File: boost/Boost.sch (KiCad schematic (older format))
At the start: 17 parts

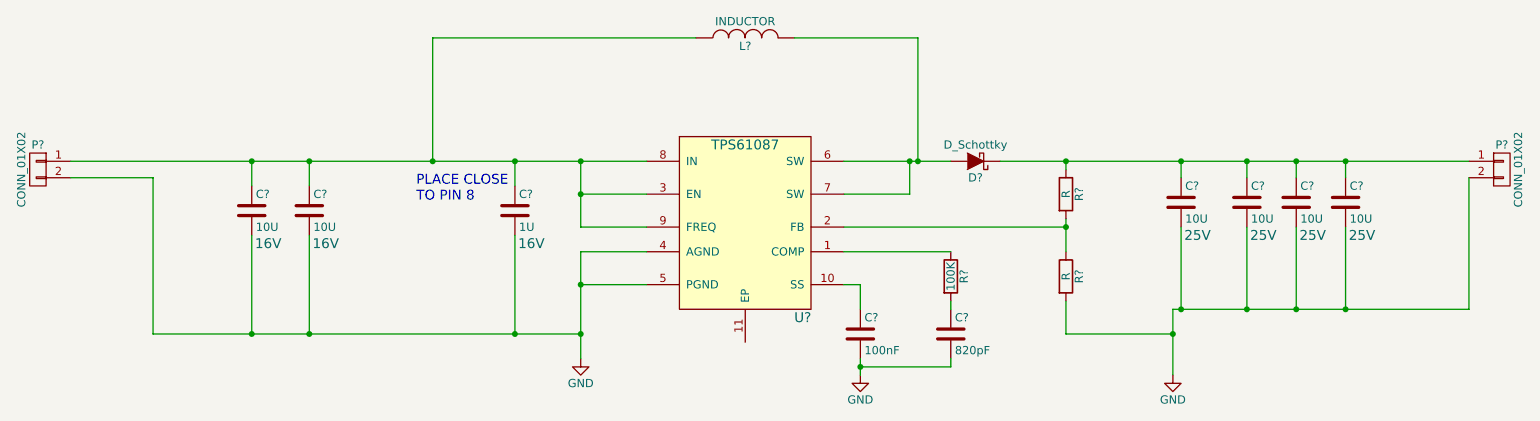
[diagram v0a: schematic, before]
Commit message: Added footprints to layout
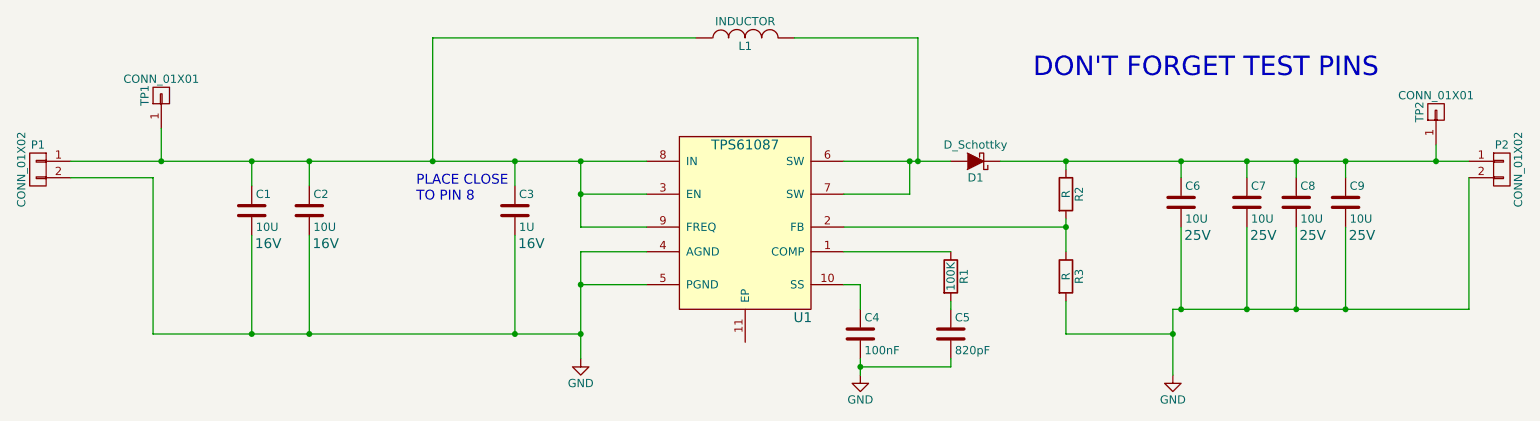
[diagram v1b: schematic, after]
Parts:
- added TP1, TP2: CONN_01X01, Measurement_Points:Measurement_Point_Square-SMD-Pad_Big, symbol CONN_01X01
- C1, C2, C6, C7, C8, C9: renamed from C?; footprint (none) -> Capacitors_SMD:C_1206_HandSoldering
- C3, C4, C5: renamed from C?; footprint (none) -> Capacitors_SMD:C_0805_HandSoldering
- D1: renamed from D?; footprint (none) -> Diodes_SMD:SMA-SMB_Universal_Handsoldering
- P1, P2: renamed from P?; footprint (none) -> Pin_Headers:Pin_Header_Straight_1x02
- R1, R2, R3: renamed from R?; footprint (none) -> Resistors_SMD:R_0805_HandSoldering
- gave numbers to parts that had none: 2
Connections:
- net at C1.1, C2.1, C3.1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: now also TP1.1 (P1)
- net at C6.1, C7.1, C8.1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: now also TP2.1 (P1)
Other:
- note added: "DON'T FORGET TEST PINS"
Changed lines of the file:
@@
 LIBS:valves
 LIBS:Boost-PowerSwap
+LIBS:Boost-cache
 EELAYER 25 0
 EELAYER END
@@
 $EndDescr
 $Comp
-L TPS61087 U?
+L TPS61087 U1
 U 1 1 56319256
 P 5600 3750
-F 0 "U?" H 5950 3200 60  0000 C CNN
+F 0 "U1" H 5950 3200 60  0000 C CNN
 F 1 "TPS61087" H 5600 4250 60  0000 C CNN
-F 2 "" H 5600 3600 60  0000 C CNN
+F 2 "" H 5600 3600 60  0001 C CNN
 F 3 "" H 5600 3600 60  0000 C CNN
 	1    5600 3750
@@
 $EndComp
 $Comp
-L INDUCTOR L?
+L INDUCTOR L1
 U 1 1 563192CC
 P 5600 2600
-F 0 "L?" V 5550 2600 50  0000 C CNN
+F 0 "L1" V 5550 2600 50  0000 C CNN
 F 1 "INDUCTOR" V 5700 2600 50  0000 C CNN
-F 2 "" H 5600 2600 60  0000 C CNN
+F 2 "" H 5600 2600 60  0001 C CNN
 F 3 "" H 5600 2600 60  0000 C CNN
 	1    5600 2600
@@
 $EndComp
 $Comp
-L GND #PWR?
+L GND #PWR01
 U 1 1 56319311
 P 4600 4550
-F 0 "#PWR?" H 4600 4300 50  0001 C CNN
+F 0 "#PWR01" H 4600 4300 50  0001 C CNN
 F 1 "GND" H 4600 4400 50  0000 C CNN
 F 2 "" H 4600 4550 60  0000 C CNN
@@
 $EndComp
 $Comp
-L C C?
+L C C1
 U 1 1 56319465
 P 2600 3650
-F 0 "C?" H 2625 3750 50  0000 L CNN
+F 0 "C1" H 2625 3750 50  0000 L CNN
 F 1 "10U" H 2625 3550 50  0000 L CNN
-F 2 "" H 2638 3500 30  0000 C CNN
+F 2 "Capacitors_SMD:C_1206_HandSoldering" H 2638 3500 30  0001 C CNN
 F 3 "" H 2600 3650 60  0000 C CNN
 F 4 "16V" H 2700 3450 60  0000 C CNN "Voltage"
@@
 $EndComp
 $Comp
-L C C?
+L C C2
 U 1 1 56319636
 P 2950 3650
-F 0 "C?" H 2975 3750 50  0000 L CNN
+F 0 "C2" H 2975 3750 50  0000 L CNN
 F 1 "10U" H 2975 3550 50  0000 L CNN
-F 2 "" H 2988 3500 30  0000 C CNN
+F 2 "Capacitors_SMD:C_1206_HandSoldering" H 2988 3500 30  0001 C CNN
 F 3 "" H 2950 3650 60  0000 C CNN
 F 4 "16V" H 3050 3450 60  0000 C CNN "Voltage"
@@
 $EndComp
 $Comp
-L C C?
+L C C3
 U 1 1 5631988E
 P 4200 3650
-F 0 "C?" H 4225 3750 50  0000 L CNN
+F 0 "C3" H 4225 3750 50  0000 L CNN
 F 1 "1U" H 4225 3550 50  0000 L CNN
-F 2 "" H 4238 3500 30  0000 C CNN
+F 2 "Capacitors_SMD:C_0805_HandSoldering" H 4238 3500 30  0001 C CNN
 F 3 "" H 4200 3650 60  0000 C CNN
 F 4 "16V" H 4300 3450 60  0000 C CNN "Voltage"
@@
 PLACE CLOSE\nTO PIN 8\n
 $Comp
-L CONN_01X02 P?
+L CONN_01X02 P1
 U 1 1 56319D59
 P 1300 3400
-F 0 "P?" H 1300 3550 50  0000 C CNN
+F 0 "P1" H 1300 3550 50  0000 C CNN
 F 1 "CONN_01X02" V 1400 3400 50  0000 C CNN
-F 2 "" H 1300 3400 60  0000 C CNN
+F 2 "Pin_Headers:Pin_Header_Straight_1x02" H 1300 3400 60  0001 C CNN
 F 3 "" H 1300 3400 60  0000 C CNN
 	1    1300 3400
@@
 $EndComp
 $Comp
-L C C?
+L C C6
 U 1 1 5631A40E
 P 8250 3600
-F 0 "C?" H 8275 3700 50  0000 L CNN
+F 0 "C6" H 8275 3700 50  0000 L CNN
 F 1 "10U" H 8275 3500 50  0000 L CNN
-F 2 "" H 8288 3450 30  0000 C CNN
+F 2 "Capacitors_SMD:C_1206_HandSoldering" H 8288 3450 30  0001 C CNN
 F 3 "" H 8250 3600 60  0000 C CNN
 F 4 "25V" H 8350 3400 60  0000 C CNN "Voltage"
@@
 $EndComp
 $Comp
-L C C?
+L C C7
 U 1 1 5631A62E
 P 8650 3600
-F 0 "C?" H 8675 3700 50  0000 L CNN
+F 0 "C7" H 8675 3700 50  0000 L CNN
 F 1 "10U" H 8675 3500 50  0000 L CNN
-F 2 "" H 8688 3450 30  0000 C CNN
+F 2 "Capacitors_SMD:C_1206_HandSoldering" H 8688 3450 30  0001 C CNN
 F 3 "" H 8650 3600 60  0000 C CNN
 F 4 "25V" H 8750 3400 60  0000 C CNN "Voltage"
@@
 $EndComp
 $Comp
-L C C?
+L C C8
 U 1 1 5631A664
 P 8950 3600
-F 0 "C?" H 8975 3700 50  0000 L CNN
+F 0 "C8" H 8975 3700 50  0000 L CNN
 F 1 "10U" H 8975 3500 50  0000 L CNN
-F 2 "" H 8988 3450 30  0000 C CNN
+F 2 "Capacitors_SMD:C_1206_HandSoldering" H 8988 3450 30  0001 C CNN
 F 3 "" H 8950 3600 60  0000 C CNN
 F 4 "25V" H 9050 3400 60  0000 C CNN "Voltage"
@@
 $EndComp
 $Comp
-L C C?
+L C C9
 U 1 1 5631A699
 P 9250 3600
-F 0 "C?" H 9275 3700 50  0000 L CNN
+F 0 "C9" H 9275 3700 50  0000 L CNN
 F 1 "10U" H 9275 3500 50  0000 L CNN
-F 2 "" H 9288 3450 30  0000 C CNN
+F 2 "Capacitors_SMD:C_1206_HandSoldering" H 9288 3450 30  0001 C CNN
 F 3 "" H 9250 3600 60  0000 C CNN
 F 4 "25V" H 9350 3400 60  0000 C CNN "Voltage"
@@
 $EndComp
 $Comp
-L GND #PWR?
+L GND #PWR02
 U 1 1 5631AB38
 P 8200 4650
-F 0 "#PWR?" H 8200 4400 50  0001 C CNN
+F 0 "#PWR02" H 8200 4400 50  0001 C CNN
 F 1 "GND" H 8200 4500 50  0000 C CNN
 F 2 "" H 8200 4650 60  0000 C CNN
@@
 $EndComp
 $Comp
-L R R?
+L R R2
 U 1 1 5631ACD8
 P 7550 3550
-F 0 "R?" V 7630 3550 50  0000 C CNN
+F 0 "R2" V 7630 3550 50  0000 C CNN
 F 1 "R" V 7550 3550 50  0000 C CNN
-F 2 "" V 7480 3550 30  0000 C CNN
+F 2 "Resistors_SMD:R_0805_HandSoldering" V 7480 3550 30  0001 C CNN
 F 3 "" H 7550 3550 30  0000 C CNN
 	1    7550 3550
@@
 $EndComp
 $Comp
-L R R?
+L R R3
 U 1 1 5631AD24
 P 7550 4050
-F 0 "R?" V 7630 4050 50  0000 C CNN
+F 0 "R3" V 7630 4050 50  0000 C CNN
 F 1 "R" V 7550 4050 50  0000 C CNN
-F 2 "" V 7480 4050 30  0000 C CNN
+F 2 "Resistors_SMD:R_0805_HandSoldering" V 7480 4050 30  0001 C CNN
 F 3 "" H 7550 4050 30  0000 C CNN
 	1    7550 4050
@@
 Connection ~ 7550 3750
 $Comp
-L C C?
+L C C4
 U 1 1 5631B263
 P 6300 4400
-F 0 "C?" H 6325 4500 50  0000 L CNN
+F 0 "C4" H 6325 4500 50  0000 L CNN
 F 1 "100nF" H 6325 4300 50  0000 L CNN
-F 2 "" H 6338 4250 30  0000 C CNN
+F 2 "Capacitors_SMD:C_0805_HandSoldering" H 6338 4250 30  0001 C CNN
 F 3 "" H 6300 4400 60  0000 C CNN
 	1    6300 4400
@@
 	6300 4100 6200 4100
 $Comp
-L GND #PWR?
+L GND #PWR03
 U 1 1 5631B351
 P 6300 4650
-F 0 "#PWR?" H 6300 4400 50  0001 C CNN
+F 0 "#PWR03" H 6300 4400 50  0001 C CNN
 F 1 "GND" H 6300 4500 50  0000 C CNN
 F 2 "" H 6300 4650 60  0000 C CNN
@@
 	6300 4550 6300 4650
 $Comp
-L C C?
+L C C5
 U 1 1 5631B401
 P 6850 4400
-F 0 "C?" H 6875 4500 50  0000 L CNN
+F 0 "C5" H 6875 4500 50  0000 L CNN
 F 1 "820pF" H 6875 4300 50  0000 L CNN
-F 2 "" H 6888 4250 30  0000 C CNN
+F 2 "Capacitors_SMD:C_0805_HandSoldering" H 6888 4250 30  0001 C CNN
 F 3 "" H 6850 4400 60  0000 C CNN
 	1    6850 4400
@@
 $EndComp
 $Comp
-L R R?
+L R R1
 U 1 1 5631B45F
 P 6850 4050
-F 0 "R?" V 6930 4050 50  0000 C CNN
+F 0 "R1" V 6930 4050 50  0000 C CNN
 F 1 "100K" V 6850 4050 50  0000 C CNN
-F 2 "" V 6780 4050 30  0000 C CNN
+F 2 "Resistors_SMD:R_0805_HandSoldering" V 6780 4050 30  0001 C CNN
 F 3 "" H 6850 4050 30  0000 C CNN
 	1    6850 4050
@@
 Connection ~ 6300 4600
 $Comp
-L D_Schottky D?
+L D_Schottky D1
 U 1 1 5631C97C
 P 7000 3350
-F 0 "D?" H 7000 3450 50  0000 C CNN
+F 0 "D1" H 7000 3450 50  0000 C CNN
 F 1 "D_Schottky" H 7000 3250 50  0000 C CNN
-F 2 "" H 7000 3350 60  0000 C CNN
+F 2 "Diodes_SMD:SMA-SMB_Universal_Handsoldering" H 7000 3350 60  0001 C CNN
 F 3 "" H 7000 3350 60  0000 C CNN
 	1    7000 3350
@@
 $EndComp
 $Comp
-L CONN_01X02 P?
+L CONN_01X02 P2
 U 1 1 5631CEDA
 P 10200 3400
-F 0 "P?" H 10200 3550 50  0000 C CNN
+F 0 "P2" H 10200 3550 50  0000 C CNN
 F 1 "CONN_01X02" V 10300 3400 50  0000 C CNN
-F 2 "" H 10200 3400 60  0000 C CNN
+F 2 "Pin_Headers:Pin_Header_Straight_1x02" H 10200 3400 60  0001 C CNN
 F 3 "" H 10200 3400 60  0000 C CNN
 	1    10200 3400
@@
 	10000 4250 10000 3450
 Connection ~ 9250 4250
+Text Notes 7350 2850 0    118  ~ 0
+DON'T FORGET TEST PINS
+$Comp
+L CONN_01X01 TP1
+U 1 1 5636B9F0
+P 2050 2950
+F 0 "TP1" H 2050 3050 50  0000 C CNN
+F 1 "CONN_01X01" V 2150 2950 50  0000 C CNN
+F 2 "Measurement_Points:Measurement_Point_Square-SMD-Pad_Big" H 2050 2950 60  0001 C CNN
+F 3 "" H 2050 2950 60  0000 C CNN
+	1    2050 2950
+	0    -1   -1   0
+$EndComp
+$Comp
+L CONN_01X01 TP2
+U 1 1 5636BC69
+P 9800 3050
+F 0 "TP2" H 9800 3150 50  0000 C CNN
+F 1 "CONN_01X01" V 9900 3050 50  0000 C CNN
+F 2 "Measurement_Points:Measurement_Point_Square-SMD-Pad_Big" H 9800 3050 60  0001 C CNN
+F 3 "" H 9800 3050 60  0000 C CNN
+	1    9800 3050
+	0    -1   -1   0
+$EndComp
+Wire Wire Line
+	9800 3250 9800 3350
+Connection ~ 9800 3350
+Wire Wire Line
+	2050 3150 2050 3350
+Connection ~ 2050 3350
 $EndSCHEMATC

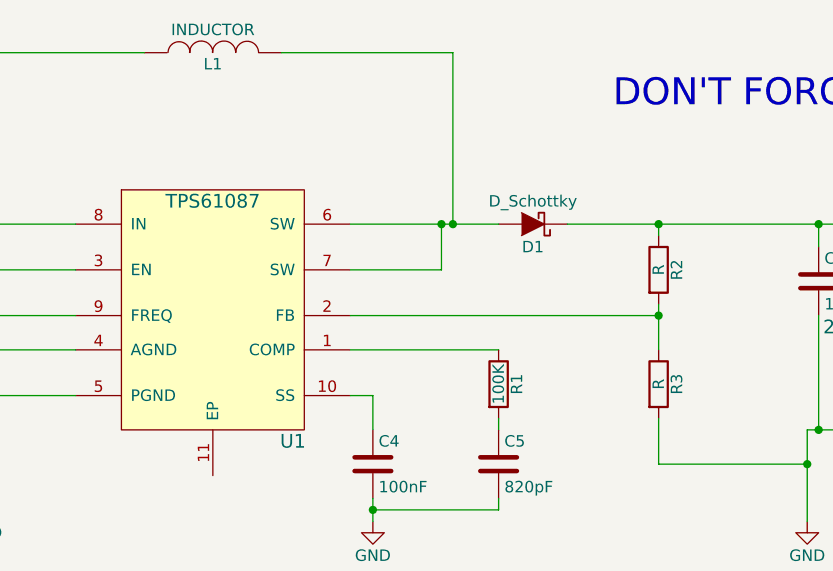
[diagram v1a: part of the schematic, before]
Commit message: Updated component values
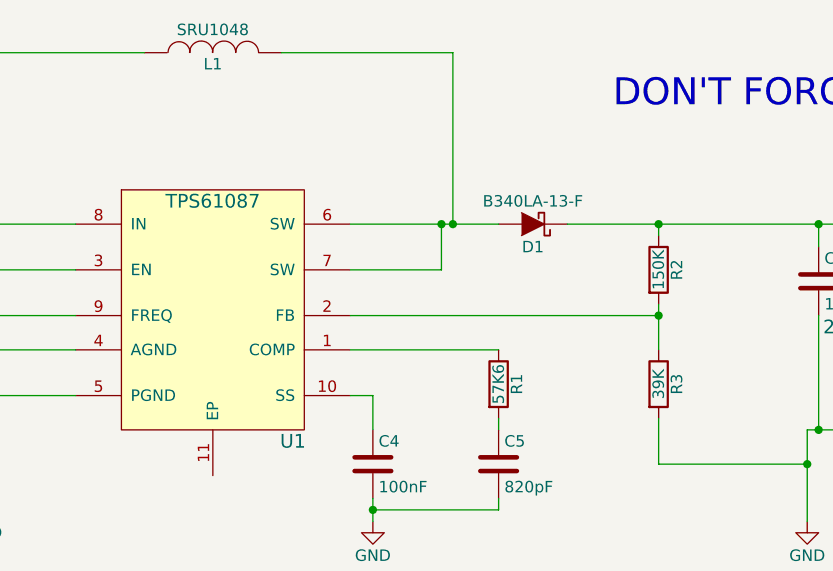
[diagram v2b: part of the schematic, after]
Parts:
- D1: value D_Schottky -> B340LA-13-F; MPN (none) -> B340LA-13-F
- L1: value INDUCTOR -> SRU1048; footprint (none) -> Boost:SRU1048; MPN (none) -> SRU1048-4R7Y
- R1: value 100K -> 57K6
- R2: value R -> 150K
- R3: value R -> 39K
- U1: footprint (none) -> Boost:TPS61087; MPN (none) -> TPS61087QDRCRQ1
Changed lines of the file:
@@
 F 0 "U1" H 5950 3200 60  0000 C CNN
 F 1 "TPS61087" H 5600 4250 60  0000 C CNN
-F 2 "" H 5600 3600 60  0001 C CNN
+F 2 "Boost:TPS61087" H 5600 3600 60  0001 C CNN
 F 3 "" H 5600 3600 60  0000 C CNN
+F 4 "TPS61087QDRCRQ1" H 5600 3750 60  0001 C CNN "MPN"
 	1    5600 3750
 	1    0    0    -1
@@
 P 5600 2600
 F 0 "L1" V 5550 2600 50  0000 C CNN
-F 1 "INDUCTOR" V 5700 2600 50  0000 C CNN
-F 2 "" H 5600 2600 60  0001 C CNN
+F 1 "SRU1048" V 5700 2600 50  0000 C CNN
+F 2 "Boost:SRU1048" H 5600 2600 60  0001 C CNN
 F 3 "" H 5600 2600 60  0000 C CNN
+F 4 "SRU1048-4R7Y" V 5600 2600 60  0001 C CNN "MPN"
 	1    5600 2600
 	0    -1   -1   0
@@
 P 7550 3550
 F 0 "R2" V 7630 3550 50  0000 C CNN
-F 1 "R" V 7550 3550 50  0000 C CNN
+F 1 "150K" V 7550 3550 50  0000 C CNN
 F 2 "Resistors_SMD:R_0805_HandSoldering" V 7480 3550 30  0001 C CNN
 F 3 "" H 7550 3550 30  0000 C CNN
@@
 P 7550 4050
 F 0 "R3" V 7630 4050 50  0000 C CNN
-F 1 "R" V 7550 4050 50  0000 C CNN
+F 1 "39K" V 7550 4050 50  0000 C CNN
 F 2 "Resistors_SMD:R_0805_HandSoldering" V 7480 4050 30  0001 C CNN
 F 3 "" H 7550 4050 30  0000 C CNN
@@
 P 6850 4050
 F 0 "R1" V 6930 4050 50  0000 C CNN
-F 1 "100K" V 6850 4050 50  0000 C CNN
+F 1 "57K6" V 6850 4050 50  0000 C CNN
 F 2 "Resistors_SMD:R_0805_HandSoldering" V 6780 4050 30  0001 C CNN
 F 3 "" H 6850 4050 30  0000 C CNN
@@
 P 7000 3350
 F 0 "D1" H 7000 3450 50  0000 C CNN
-F 1 "D_Schottky" H 7000 3250 50  0000 C CNN
+F 1 "B340LA-13-F" H 7000 3250 50  0000 C CNN
 F 2 "Diodes_SMD:SMA-SMB_Universal_Handsoldering" H 7000 3350 60  0001 C CNN
 F 3 "" H 7000 3350 60  0000 C CNN
+F 4 "B340LA-13-F" H 7000 3350 60  0001 C CNN "MPN"
 	1    7000 3350
 	-1   0    0    1

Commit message: Initial Layout
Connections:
- net GND: now also U1.11 (EP)
- net Vin: now reaches C1.1, C2.1, C3.1, L1.1, P1.1 (P1), TP1.1 (P1), U1.3 (EN), U1.8 (IN), U1.9 (FREQ)
- net SW: now reaches D1.2 (A), L1.2, U1.6 (SW), U1.7 (SW)
- net Vout: now reaches C6.1, C7.1, C8.1, C9.1, D1.1 (K), P2.1 (P1), R2.1, TP2.1 (P1)
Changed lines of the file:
@@
 	2050 3150 2050 3350
 Connection ~ 2050 3350
+Wire Wire Line
+	4600 4500 5600 4500
+Wire Wire Line
+	5600 4500 5600 4450
+Connection ~ 4600 4500
+Text Label 6250 3350 0    60   ~ 0
+SW
+Text Label 3200 3350 0    60   ~ 0
+Vin
+Text Label 7900 3350 0    60   ~ 0
+Vout
 $EndSCHEMATC

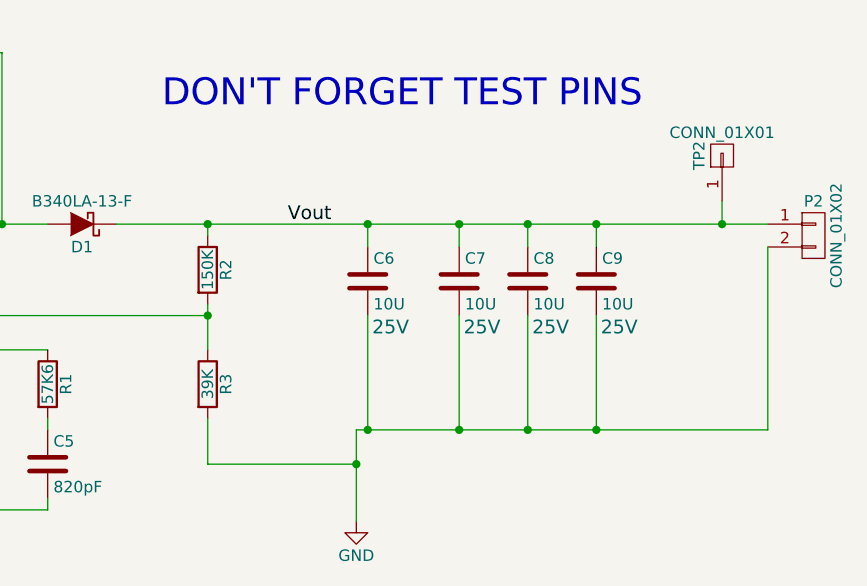
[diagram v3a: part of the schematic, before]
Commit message: Added indicator LED, mounting holes and a logo.
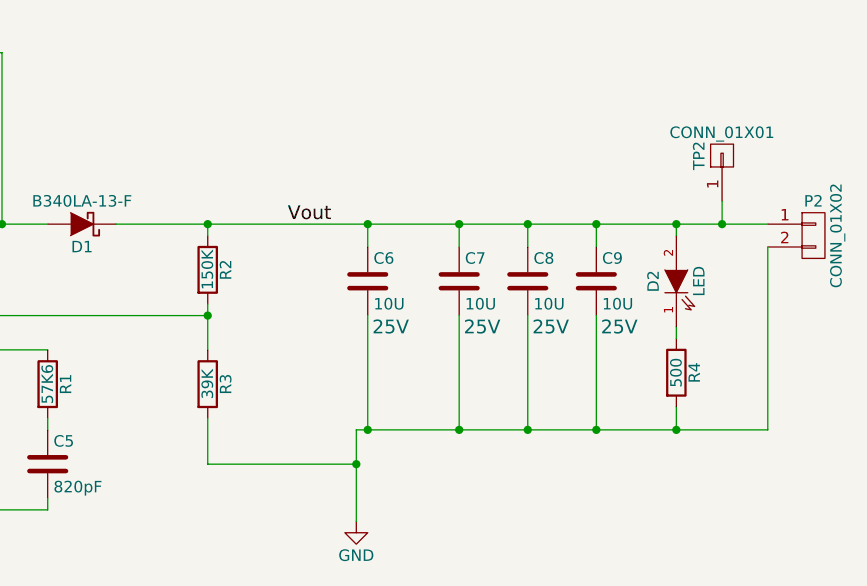
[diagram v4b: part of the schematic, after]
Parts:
- added D2: LED, LEDs:LED-0805, symbol LED
- added R4: 500, Resistors_SMD:R_0805_HandSoldering, symbol R
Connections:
- net GND: now also R4.2
- net Vout: now also D2.2 (A)
- new net: D2.1 (K), R4.1
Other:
- note removed: "DON'T FORGET TEST PINS"
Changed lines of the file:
@@
 	10000 4250 10000 3450
 Connection ~ 9250 4250
-Text Notes 7350 2850 0    118  ~ 0
-DON'T FORGET TEST PINS
 $Comp
 L CONN_01X01 TP1
@@
 Text Label 7900 3350 0    60   ~ 0
 Vout
+$Comp
+L LED D2
+U 1 1 563F9E2F
+P 9600 3600
+F 0 "D2" H 9600 3700 50  0000 C CNN
+F 1 "LED" H 9600 3500 50  0000 C CNN
+F 2 "LEDs:LED-0805" H 9600 3600 60  0001 C CNN
+F 3 "" H 9600 3600 60  0000 C CNN
+	1    9600 3600
+	0    -1   -1   0
+$EndComp
+$Comp
+L R R4
+U 1 1 563F9F12
+P 9600 4000
+F 0 "R4" V 9680 4000 50  0000 C CNN
+F 1 "500" V 9600 4000 50  0000 C CNN
+F 2 "Resistors_SMD:R_0805_HandSoldering" V 9530 4000 30  0001 C CNN
+F 3 "" H 9600 4000 30  0000 C CNN
+	1    9600 4000
+	1    0    0    -1
+$EndComp
+Wire Wire Line
+	9600 3350 9600 3400
+Connection ~ 9600 3350
+Wire Wire Line
+	9600 3800 9600 3850
+Wire Wire Line
+	9600 4150 9600 4250
+Connection ~ 9600 4250
 $EndSCHEMATC
